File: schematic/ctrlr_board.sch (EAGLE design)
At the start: 19 parts, among them K1 SRLY-19, K2 SRLY-19, K3 SRLY-19, K4 SRLY-19, K5 SRLY-19, K6 SRLY-19

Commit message: V1.0 of relay board
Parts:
- removed POWER: (no value), con-lstb:MA10-1
- added PWR: 10X1, dz:10X1
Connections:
- net HOT: now also PWR.1; no longer POWER.1
- net N$10: now also PWR.6; no longer POWER.6
- net N$11: now also PWR.7; no longer POWER.7
- net N$12: now also PWR.2; no longer POWER.2
- net N$7: now also PWR.3; no longer POWER.3
- net N$8: now also PWR.4; no longer POWER.4
- net N$9: now also PWR.5; no longer POWER.5
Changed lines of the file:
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@@
 <parts>
 <part name="2803" library="uln-udn" deviceset="ULN2803A" device=""/>
-<part name="POWER" library="con-lstb" deviceset="MA10-1" device=""/>
 <part name="TEMP" library="dz" deviceset="3X1" device=""/>
 <part name="RPI_HDR" library="dz" deviceset="RASPBERRY_PI_HEADER" device="RASPI_HDR"/>
@@
 <part name="RELAY6" library="dz" deviceset="2X1" device="+-"/>
 <part name="K1" library="dz" deviceset="SRLY-19" device=""/>
+<part name="PWR" library="dz" deviceset="10X1" device=""/>
 </parts>
 <sheets>
@@
 <instances>
 <instance part="2803" gate="G$1" x="71.12" y="86.36"/>
-<instance part="POWER" gate="1" x="187.96" y="106.68" rot="R180"/>
 <instance part="TEMP" gate="G$1" x="43.18" y="109.22"/>
 <instance part="RPI_HDR" gate="G$1" x="73.66" y="48.26"/>
@@
 <instance part="RELAY6" gate="G$1" x="205.74" y="63.5"/>
 <instance part="K1" gate="G$1" x="134.62" y="114.3"/>
+<instance part="PWR" gate="G$1" x="187.96" y="104.14" rot="R180"/>
 </instances>
 <busses>
@@
 <net name="HOT" class="0">
 <segment>
-<pinref part="POWER" gate="1" pin="1"/>
 <wire x1="180.34" y1="116.84" x2="144.78" y2="116.84" width="0.1524" layer="91"/>
 <label x="152.4" y="116.84" size="1.778" layer="95"/>
 <pinref part="K1" gate="G$1" pin="D1"/>
+<pinref part="PWR" gate="G$1" pin="1"/>
 </segment>
 <segment>
@@
 <wire x1="144.78" y1="93.98" x2="157.48" y2="93.98" width="0.1524" layer="91"/>
 <wire x1="157.48" y1="93.98" x2="157.48" y2="111.76" width="0.1524" layer="91"/>
-<pinref part="POWER" gate="1" pin="3"/>
 <wire x1="157.48" y1="111.76" x2="180.34" y2="111.76" width="0.1524" layer="91"/>
 <pinref part="K2" gate="G$1" pin="D2"/>
+<pinref part="PWR" gate="G$1" pin="3"/>
 </segment>
 </net>
@@
 <wire x1="144.78" y1="78.74" x2="160.02" y2="78.74" width="0.1524" layer="91"/>
 <wire x1="160.02" y1="78.74" x2="160.02" y2="109.22" width="0.1524" layer="91"/>
-<pinref part="POWER" gate="1" pin="4"/>
 <wire x1="180.34" y1="109.22" x2="160.02" y2="109.22" width="0.1524" layer="91"/>
 <pinref part="K3" gate="G$1" pin="D2"/>
+<pinref part="PWR" gate="G$1" pin="4"/>
 </segment>
 </net>
@@
 <wire x1="162.56" y1="106.68" x2="162.56" y2="63.5" width="0.1524" layer="91"/>
 <wire x1="162.56" y1="63.5" x2="144.78" y2="63.5" width="0.1524" layer="91"/>
-<pinref part="POWER" gate="1" pin="5"/>
 <wire x1="162.56" y1="106.68" x2="180.34" y2="106.68" width="0.1524" layer="91"/>
 <pinref part="K4" gate="G$1" pin="D2"/>
+<pinref part="PWR" gate="G$1" pin="5"/>
 </segment>
 </net>
@@
 <wire x1="144.78" y1="48.26" x2="165.1" y2="48.26" width="0.1524" layer="91"/>
 <wire x1="165.1" y1="48.26" x2="165.1" y2="104.14" width="0.1524" layer="91"/>
-<pinref part="POWER" gate="1" pin="6"/>
 <wire x1="180.34" y1="104.14" x2="165.1" y2="104.14" width="0.1524" layer="91"/>
 <pinref part="K5" gate="G$1" pin="D2"/>
+<pinref part="PWR" gate="G$1" pin="6"/>
 </segment>
 </net>
@@
 <wire x1="167.64" y1="101.6" x2="167.64" y2="33.02" width="0.1524" layer="91"/>
 <wire x1="167.64" y1="33.02" x2="144.78" y2="33.02" width="0.1524" layer="91"/>
-<pinref part="POWER" gate="1" pin="7"/>
 <wire x1="167.64" y1="101.6" x2="180.34" y2="101.6" width="0.1524" layer="91"/>
 <pinref part="K6" gate="G$1" pin="D2"/>
+<pinref part="PWR" gate="G$1" pin="7"/>
 </segment>
 </net>
 <net name="N$12" class="0">
 <segment>
-<pinref part="POWER" gate="1" pin="2"/>
 <wire x1="180.34" y1="114.3" x2="154.94" y2="114.3" width="0.1524" layer="91"/>
 <wire x1="154.94" y1="114.3" x2="154.94" y2="111.76" width="0.1524" layer="91"/>
 <wire x1="154.94" y1="111.76" x2="144.78" y2="111.76" width="0.1524" layer="91"/>
 <pinref part="K1" gate="G$1" pin="D2"/>
-</segment>
-</net>
+<pinref part="PWR" gate="G$1" pin="2"/>
+</segment>
+</net>

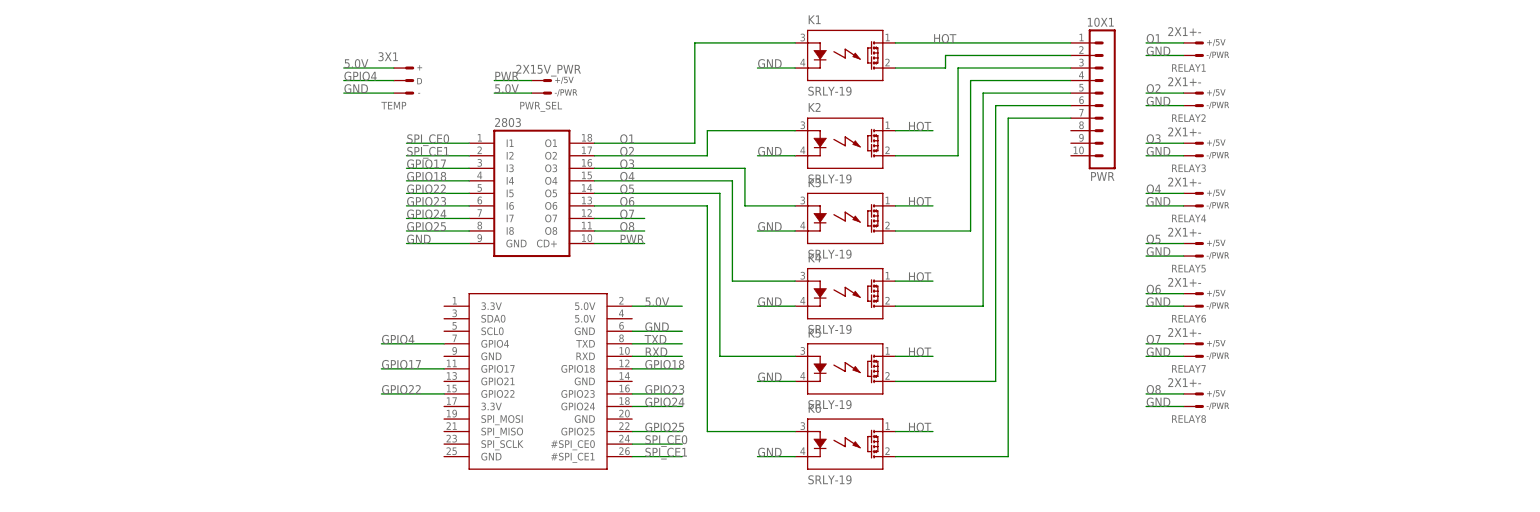
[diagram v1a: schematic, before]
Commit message: Version 1.1 of expansion board
  * Rotated header 180 so expansion board sits over Rpi
  * re-wired relays to switch GND via darlingtons
  * Added optional SMD LEDs to relays 1-6 for testing
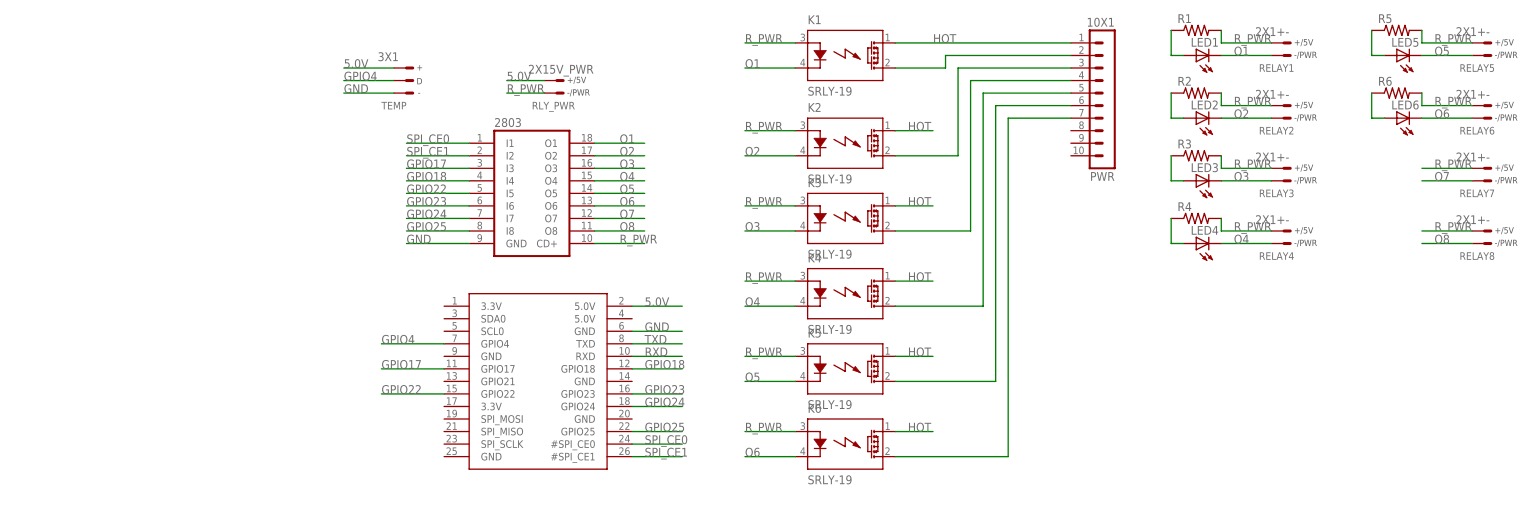
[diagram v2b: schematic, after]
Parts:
- removed PWR_SEL: 2X15V_PWR, dz:2X15V_PWR
- added LED1, LED2, LED3, LED4, LED5, LED6: (no value), led:LEDCHIPLED_0603
- added R1, R2, R3, R4, R5, R6: (no value), resistor:R-US_R0603
- added RLY_PWR: 2X15V_PWR, dz:2X15V_PWR
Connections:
- removed net PWR: 2803.CD+, PWR_SEL.+
- new net N$1: LED1.A, R1.1
- new net N$2: LED2.A, R2.1
- new net N$3: LED3.A, R3.1
- new net N$4: LED4.A, R4.1
- new net N$5: LED5.A, R5.1
- new net N$6: LED6.A, R6.1
- new net R_PWR: 2803.CD+, K1.A, K2.A, K3.A, K4.A, K5.A, K6.A, R1.2, R2.2, R3.2, R4.2, R5.2, R6.2, RELAY1.+, RELAY2.+, RELAY3.+, RELAY4.+, RELAY5.+, RELAY6.+, RELAY7.+, RELAY8.+, RLY_PWR.-
- net 5.0V: now also RLY_PWR.+; no longer PWR_SEL.-
- net GND: no longer K1.K, K2.K, K3.K, K4.K, K5.K, K6.K, RELAY1.-, RELAY2.-, RELAY3.-, RELAY4.-, RELAY5.-, RELAY6.-, RELAY7.-, RELAY8.-
- net O1: now also K1.K, LED1.C, RELAY1.-; no longer K1.A, RELAY1.+
- net O2: now also K2.K, LED2.C, RELAY2.-; no longer K2.A, RELAY2.+
- net O3: now also K3.K, LED3.C, RELAY3.-; no longer K3.A, RELAY3.+
- net O4: now also K4.K, LED4.C, RELAY4.-; no longer K4.A, RELAY4.+
- net O5: now also K5.K, LED5.C, RELAY5.-; no longer K5.A, RELAY5.+
- net O6: now also K6.K, LED6.C, RELAY6.-; no longer K6.A, RELAY6.+
- net O7: now also RELAY7.-; no longer RELAY7.+
- net O8: now also RELAY8.-; no longer RELAY8.+
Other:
- moved on the sheet: RELAY1, RELAY2, RELAY3, RELAY4, RELAY5, RELAY6, RELAY7, RELAY8

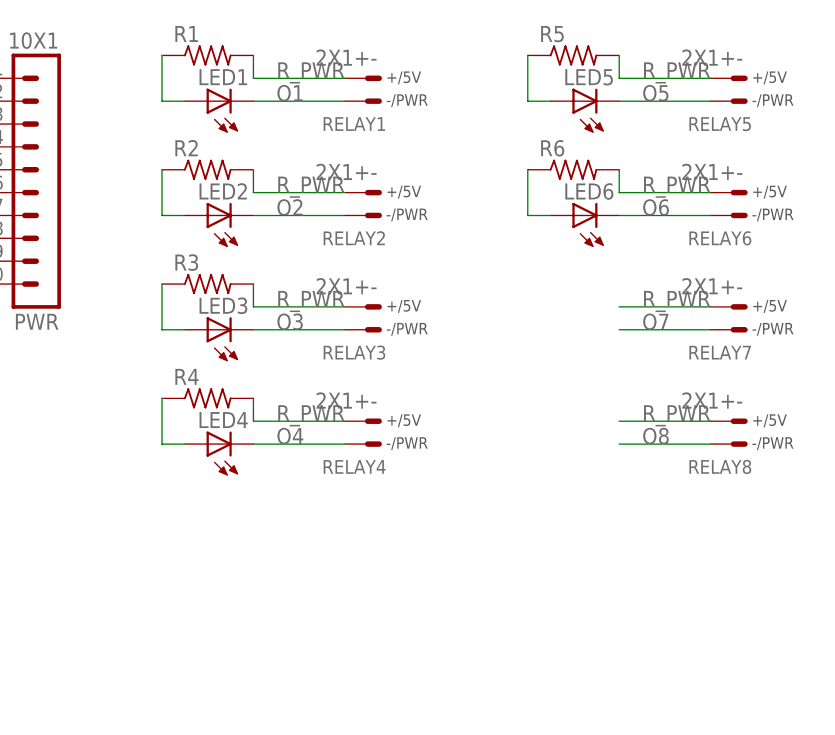
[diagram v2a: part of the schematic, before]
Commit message: Version 1.1b of expansion board
  * v. 1.1 failed batchpcb DRC.
  * Re-did layout by hand
  * Added larger solder pads on relays
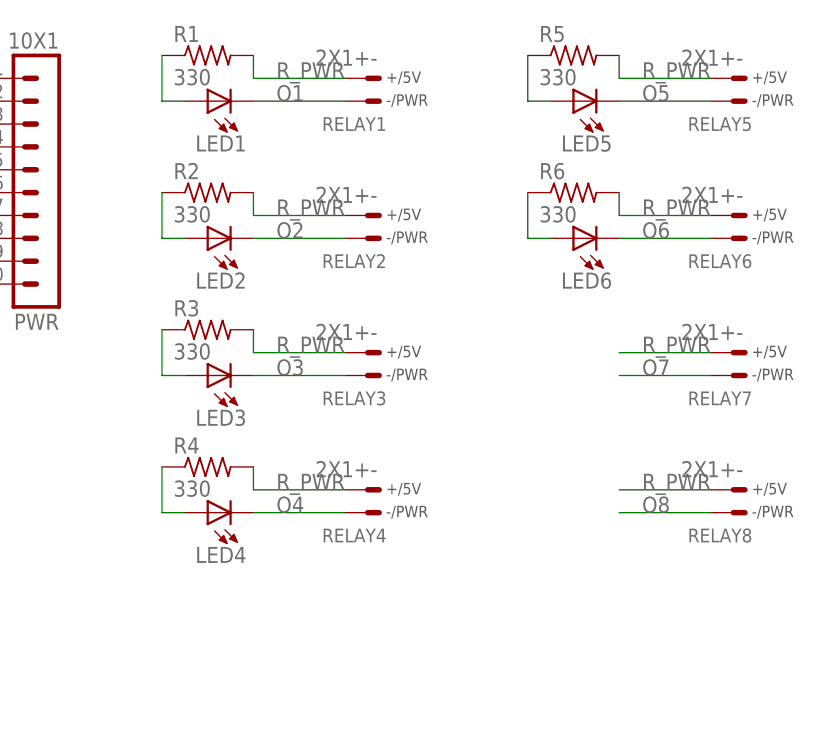
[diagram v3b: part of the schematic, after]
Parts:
- LED1, LED2, LED3, LED4, LED5, LED6: value (none) -> LED; device led:LEDCHIPLED_0603 -> dz:LED
- R1, R2, R3, R4, R5, R6: value (none) -> 330; device resistor:R-US_R0603 -> dz:RESISTOR
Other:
- moved on the sheet: LED2, LED3, LED4, LED6, R2, R3, R4, R6, RELAY2, RELAY3, RELAY4, RELAY6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

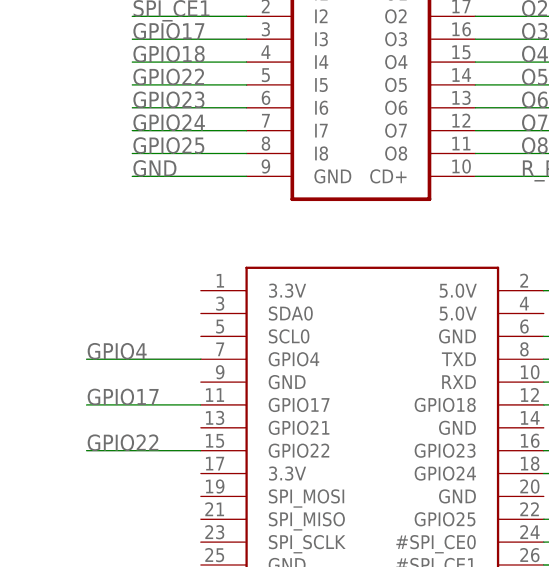
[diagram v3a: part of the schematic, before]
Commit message: Version 1.1c of expansion board
  * v. 1.1b failed batchpcb DRC (SFE DRC rules were the problem)
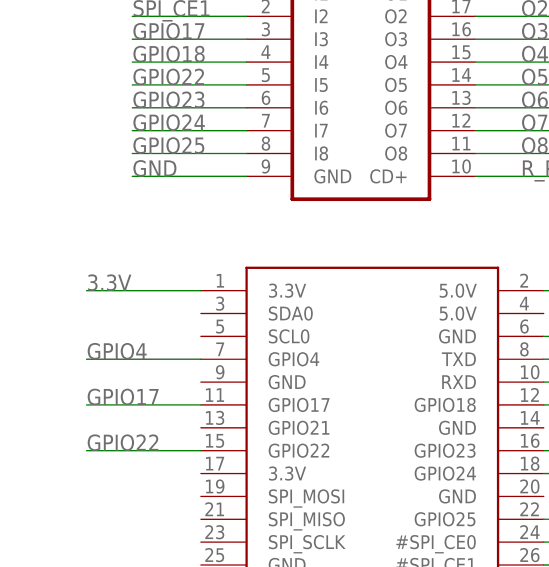
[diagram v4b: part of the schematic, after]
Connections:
- new net 3.3V: RPI_HDR.3.3V@1
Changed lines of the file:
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@@
+</segment>
+</net>
+<net name="3.3V" class="0">
+<segment>
+<pinref part="RPI_HDR" gate="G$1" pin="3.3V@1"/>
+<wire x1="53.34" y1="63.5" x2="40.64" y2="63.5" width="0.1524" layer="91"/>
+<label x="40.64" y="63.5" size="1.778" layer="95"/>
 </segment>
 </net>

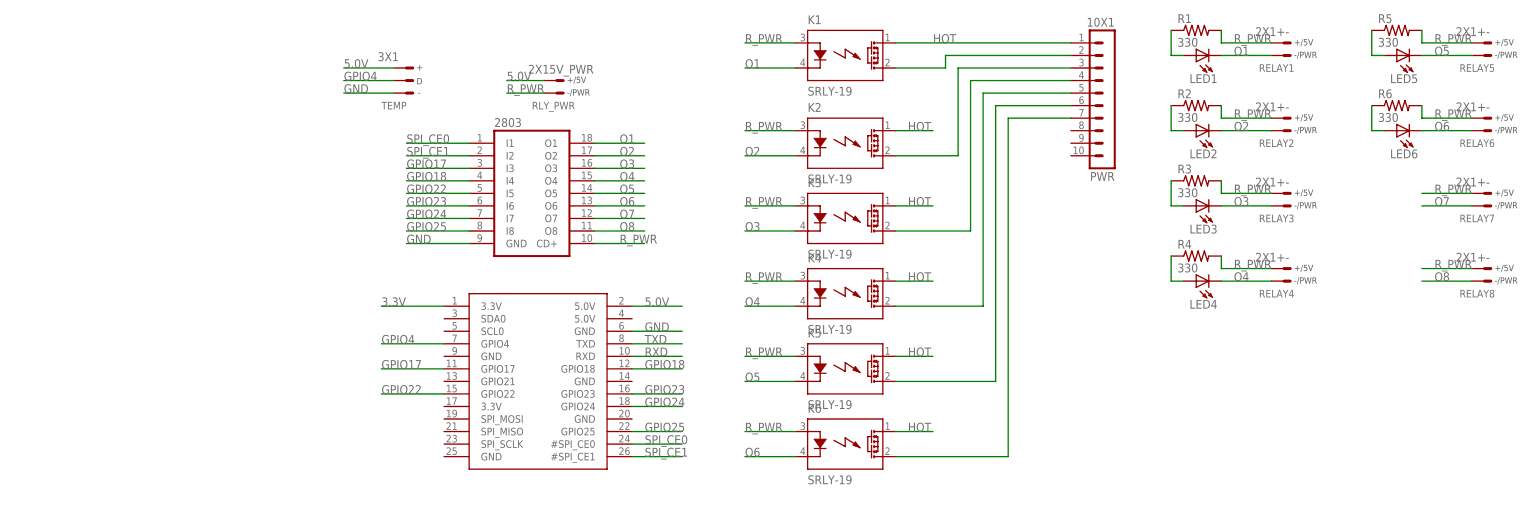
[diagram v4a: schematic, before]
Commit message: Board updates for V2.0 hardware
BatchPCB went out of business so switching to oshpark.com.
Removed gerber files since they aren't needed there.  V2.0 has
the following changes:
 * Replace darlington array with 3 WS2801 to do PWM in hardware
 * Add 9th relay output
 * silkscreen high voltage area
 * Add pullup on one wire bus
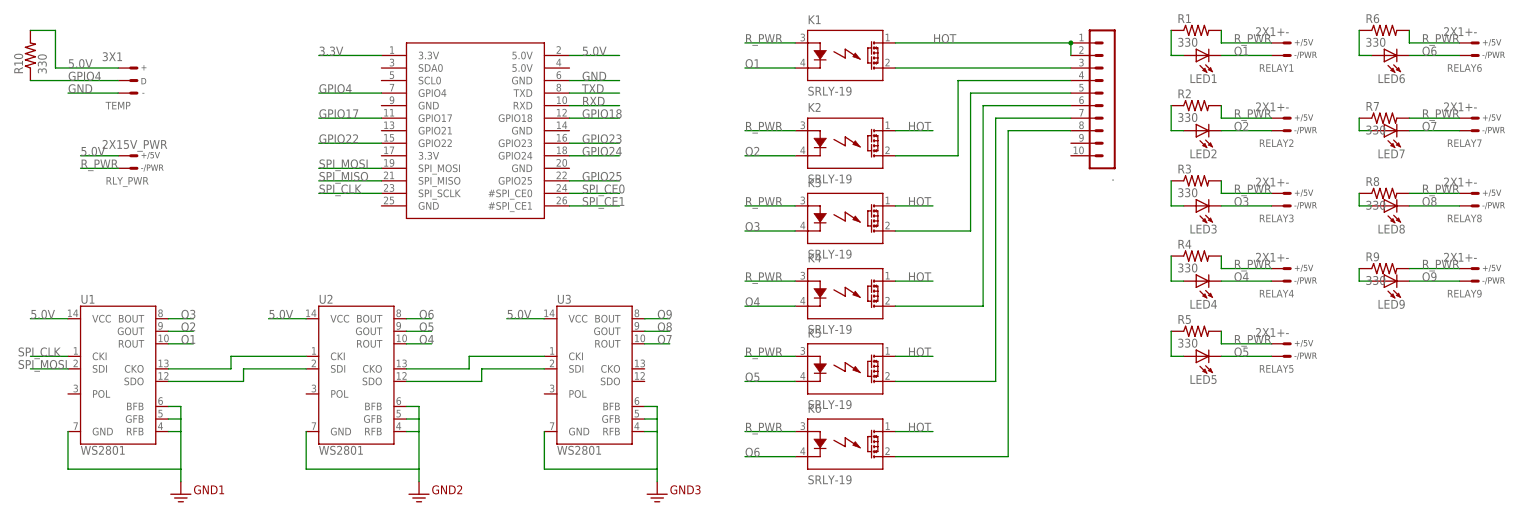
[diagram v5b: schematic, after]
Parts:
- removed 2803: (no value), uln-udn:ULN2803A
- added LED7, LED8, LED9: LED, dz:LED
- added R10, R7, R8, R9: 330, dz:RESISTOR
- added RELAY9: 2X1+-, dz:2X1+-
- added U1, U2, U3: WS2801, SparkFun-DigitalIC:WS2801
- renumbered PWR to .
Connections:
- new net N$13: LED7.A, R7.1
- new net N$14: LED8.A, R8.1
- new net N$15: U1.CKO, U2.CKI
- new net N$16: U1.SDO, U2.SDI
- new net N$17: U2.SDO, U3.SDI
- new net N$18: U2.CKO, U3.CKI
- new net N$19: LED9.A, R9.1
- new net O9: LED9.C, RELAY9.-, U3.BOUT
- new net SPI_CLK: RPI_HDR.SPI_SCLK, U1.CKI
- new net SPI_MISO: RPI_HDR.SPI_MISO
- new net SPI_MOSI: RPI_HDR.SPI_MOSI, U1.SDI
- net 5.0V: now also R10.2, U1.VCC, U2.VCC, U3.VCC
- net GND: now also U1.BFB, U1.GFB, U1.GND, U1.RFB, U2.BFB, U2.GFB, U2.GND, U2.RFB, U3.BFB, U3.GFB, U3.GND, U3.RFB; no longer 2803.GND
- net GPIO17: no longer 2803.I3
- net GPIO18: no longer 2803.I4
- net GPIO22: no longer 2803.I5
- net GPIO23: no longer 2803.I6
- net GPIO24: no longer 2803.I7
- net GPIO25: no longer 2803.I8
- net GPIO4: now also R10.1
- net HOT: now also ..2
- net N$10: now also ..7; no longer ..6
- net N$11: now also ..8; no longer ..7
- net N$12: now also ..3; no longer ..2
- net N$7: now also ..4; no longer ..3
- net N$8: now also ..5; no longer ..4
- net N$9: now also ..6; no longer ..5
- net O1: now also U1.ROUT; no longer 2803.O1
- net O2: now also U1.GOUT; no longer 2803.O2
- net O3: now also U1.BOUT; no longer 2803.O3
- net O4: now also U2.ROUT; no longer 2803.O4
- net O5: now also U2.GOUT; no longer 2803.O5
- net O6: now also U2.BOUT; no longer 2803.O6
- net O7: now also LED7.C, U3.ROUT; no longer 2803.O7
- net O8: now also LED8.C, U3.GOUT; no longer 2803.O8
- net R_PWR: now also R7.2, R8.2, R9.2, RELAY9.+; no longer 2803.CD+
- net SPI_CE0: no longer 2803.I1
- net SPI_CE1: no longer 2803.I2
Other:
- moved on the sheet: LED5, LED6, R5, R6, RELAY5, RELAY6, RELAY7, RELAY8, RLY_PWR, TEMP
